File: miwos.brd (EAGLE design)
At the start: 120 x 120 mm, 50 parts, among them J1 614004190021, U1 PEC16, U3 PEC16

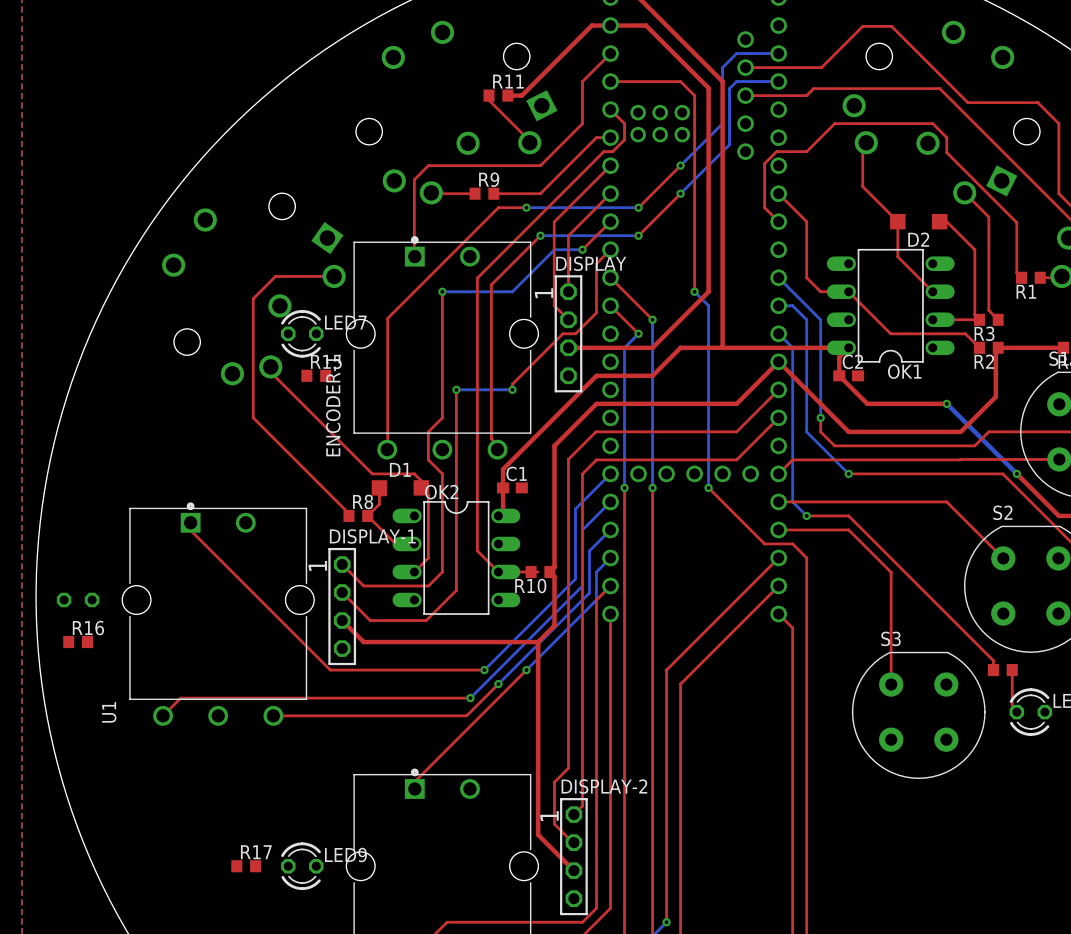
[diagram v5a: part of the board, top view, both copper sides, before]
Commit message: Wire encoder LEDs
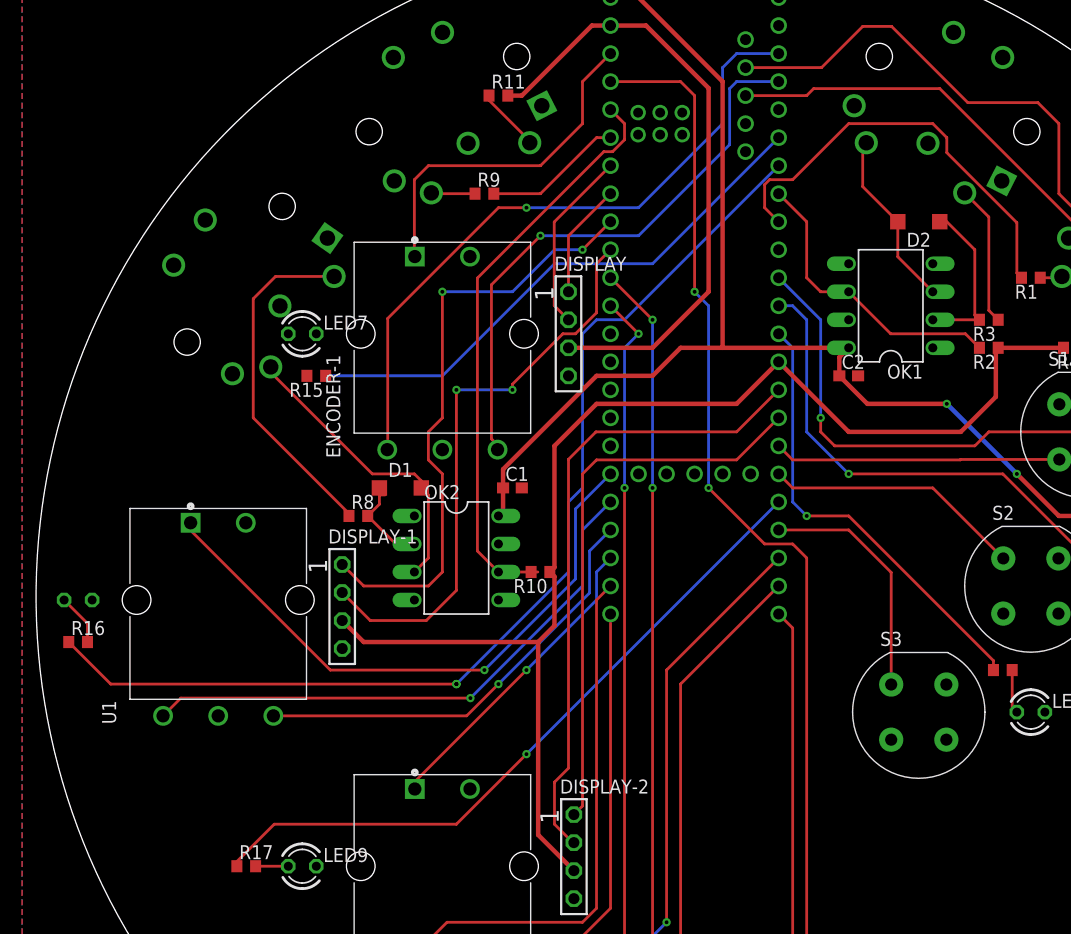
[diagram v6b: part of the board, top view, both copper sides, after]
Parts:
- turned R15 to 180 degrees
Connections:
- net BUTTON-1: now also TEENSY-41.26; no longer TEENSY-41.27
- net BUTTON-2: now also TEENSY-41.27; no longer TEENSY-41.28
- net ENCODER-1-LED: now also TEENSY-41.5
- net ENCODER-2-LED: now also TEENSY-41.6
- net ENCODER-3-LED: now also TEENSY-41.28
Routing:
- net ENCODER-2-LED: track 0.00 -> 97.3 mm, vias 0 -> 2
- net ENCODER-3-LED: track 0.00 -> 63.0 mm, vias 0 -> 1
- net ENCODER-1-LED: track 0.00 -> 49.6 mm
- net N$20: track 0.00 -> 4.69 mm
- net N$22: track 0.00 -> 2.96 mm
- net TX-2: track 39.8 -> 38.7 mm
- net BUTTON-2: track 22.5 -> 23.5 mm
- net ENCODER-1-B: vias 3 -> 1
- net ENCODER-1-A: vias 3 -> 1
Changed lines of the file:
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@@
 <attribute name="VALUE" x="26.035" y="82.169" size="1.27" layer="27" ratio="10"/>
 </element>
-<element name="R15" library="rcl" library_urn="urn:adsk.eagle:library:334" package="R0603" package3d_urn="urn:adsk.eagle:package:23555/3" value="220R" x="25.4" y="80.01" smashed="yes">
-<attribute name="NAME" x="24.765" y="80.645" size="1.27" layer="25"/>
-<attribute name="POPULARITY" value="70" x="25.4" y="76.2" size="1.778" layer="27" display="off"/>
-<attribute name="SPICEPREFIX" value="R" x="25.4" y="76.2" size="1.778" layer="27" display="off"/>
-<attribute name="VALUE" x="24.765" y="78.105" size="1.27" layer="27"/>
+<element name="R15" library="rcl" library_urn="urn:adsk.eagle:library:334" package="R0603" package3d_urn="urn:adsk.eagle:package:23555/3" value="220R" x="25.4" y="80.01" smashed="yes" rot="R180">
+<attribute name="NAME" x="26.035" y="79.375" size="1.27" layer="25" rot="R180"/>
+<attribute name="POPULARITY" value="70" x="25.4" y="83.82" size="1.778" layer="27" rot="R180" display="off"/>
+<attribute name="SPICEPREFIX" value="R" x="25.4" y="83.82" size="1.778" layer="27" rot="R180" display="off"/>
+<attribute name="VALUE" x="26.035" y="81.915" size="1.27" layer="27" rot="R180"/>
 </element>
 <element name="LED8" library="led" library_urn="urn:adsk.eagle:library:259" package="LED3MM" package3d_urn="urn:adsk.eagle:package:15797/1" value="" x="3.81" y="59.69" smashed="yes" rot="MR180">
@@
 <wire x1="41.91" y1="95.25" x2="44.45" y2="95.25" width="0.254" layer="1"/>
 <via x="44.45" y="95.25" extent="1-16" drill="0.35"/>
-<wire x1="44.45" y1="95.25" x2="54.61" y2="95.25" width="0.254" layer="16"/>
-<via x="54.61" y="95.25" extent="1-16" drill="0.35"/>
-<wire x1="54.61" y1="95.25" x2="58.42" y2="99.06" width="0.254" layer="1"/>
-<via x="58.42" y="99.06" extent="1-16" drill="0.35"/>
-<wire x1="58.42" y1="99.06" x2="62.23" y2="102.87" width="0.254" layer="16"/>
-<wire x1="62.23" y1="102.87" x2="62.23" y2="107.95" width="0.254" layer="16"/>
+<wire x1="54.61" y1="95.25" x2="44.45" y2="95.25" width="0.254" layer="16"/>
+<wire x1="62.23" y1="107.95" x2="62.23" y2="102.87" width="0.254" layer="16"/>
 <wire x1="62.23" y1="107.95" x2="63.5" y2="109.22" width="0.254" layer="16"/>
 <wire x1="63.5" y1="109.22" x2="67.31" y2="109.22" width="0.254" layer="16"/>
+<wire x1="62.23" y1="102.87" x2="54.61" y2="95.25" width="0.254" layer="16"/>
 </signal>
 <signal name="ENCODER-1-B">
@@
 <via x="45.72" y="92.71" extent="1-16" drill="0.35"/>
 <wire x1="45.72" y1="92.71" x2="54.61" y2="92.71" width="0.254" layer="16"/>
-<via x="54.61" y="92.71" extent="1-16" drill="0.35"/>
-<wire x1="54.61" y1="92.71" x2="58.42" y2="96.52" width="0.254" layer="1"/>
-<via x="58.42" y="96.52" extent="1-16" drill="0.35"/>
-<wire x1="58.42" y1="96.52" x2="62.865" y2="100.965" width="0.254" layer="16"/>
 <wire x1="62.865" y1="106.045" x2="63.5" y2="106.68" width="0.254" layer="16"/>
 <wire x1="63.5" y1="106.68" x2="67.31" y2="106.68" width="0.254" layer="16"/>
 <wire x1="62.865" y1="100.965" x2="62.865" y2="106.045" width="0.254" layer="16"/>
+<wire x1="54.61" y1="92.71" x2="62.865" y2="100.965" width="0.254" layer="16"/>
 </signal>
 <signal name="ENCODER-1-PUSH">
@@
 <contactref element="S1" pad="1"/>
 <contactref element="S1" pad="2"/>
-<contactref element="TEENSY-41" pad="27"/>
 <wire x1="92.75" y1="72.43" x2="83.82" y2="72.43" width="0.254" layer="1"/>
-<wire x1="83.78" y1="72.39" x2="68.58" y2="72.39" width="0.254" layer="1"/>
-<wire x1="67.31" y1="71.12" x2="68.58" y2="72.39" width="0.254" layer="1"/>
+<wire x1="68.58" y1="72.39" x2="83.78" y2="72.39" width="0.254" layer="1"/>
 <wire x1="83.78" y1="72.39" x2="83.82" y2="72.43" width="0.254" layer="1"/>
+<contactref element="TEENSY-41" pad="26"/>
+<wire x1="67.31" y1="73.66" x2="68.58" y2="72.39" width="0.254" layer="1"/>
 <wire x1="92.75" y1="72.43" x2="92.75" y2="77.43" width="0" layer="19" extent="1-1"/>
 </signal>
@@
 <contactref element="S2" pad="1"/>
 <contactref element="S2" pad="2"/>
-<wire x1="85.09" y1="66.04" x2="87.63" y2="63.5" width="0.254" layer="1"/>
-<contactref element="TEENSY-41" pad="28"/>
-<wire x1="87.63" y1="63.5" x2="87.67" y2="63.46" width="0.254" layer="1"/>
-<wire x1="67.31" y1="68.58" x2="82.55" y2="68.58" width="0.254" layer="1"/>
-<wire x1="82.55" y1="68.58" x2="85.09" y2="66.04" width="0.254" layer="1"/>
+<wire x1="87.67" y1="63.46" x2="81.28" y2="69.85" width="0.254" layer="1"/>
+<contactref element="TEENSY-41" pad="27"/>
+<wire x1="68.58" y1="69.85" x2="67.31" y2="71.12" width="0.254" layer="1"/>
+<wire x1="81.28" y1="69.85" x2="68.58" y2="69.85" width="0.254" layer="1"/>
 <wire x1="87.67" y1="63.46" x2="87.67" y2="58.46" width="0" layer="19" extent="1-1"/>
 </signal>
@@
 <wire x1="66.04" y1="95.25" x2="67.31" y2="93.98" width="0.254" layer="1"/>
 <wire x1="82.55" y1="101.6" x2="82.55" y2="100.242" width="0.254" layer="1"/>
-<wire x1="72.39" y1="102.87" x2="81.28" y2="102.87" width="0.254" layer="1"/>
+<wire x1="73.66" y1="102.87" x2="81.28" y2="102.87" width="0.254" layer="1"/>
 <wire x1="81.28" y1="102.87" x2="82.55" y2="101.6" width="0.254" layer="1"/>
-<wire x1="72.39" y1="102.87" x2="69.85" y2="100.33" width="0.254" layer="1"/>
-<wire x1="67.11855" y1="100.33" x2="66.04" y2="99.25145" width="0.254" layer="1"/>
-<wire x1="69.85" y1="100.33" x2="67.11855" y2="100.33" width="0.254" layer="1"/>
-<wire x1="66.04" y1="99.25145" x2="66.04" y2="95.25" width="0.254" layer="1"/>
+<wire x1="73.66" y1="102.87" x2="68.58" y2="97.79" width="0.254" layer="1"/>
+<wire x1="66.48355" y1="97.79" x2="66.04" y2="97.34645" width="0.254" layer="1"/>
+<wire x1="68.58" y1="97.79" x2="66.48355" y2="97.79" width="0.254" layer="1"/>
+<wire x1="66.04" y1="97.34645" x2="66.04" y2="95.25" width="0.254" layer="1"/>
 </signal>
 <signal name="BUTTON-4-LED">
@@
 <contactref element="LED7" pad="A"/>
 <contactref element="R15" pad="2"/>
-<wire x1="26.25" y1="80.01" x2="22.86" y2="83.82" width="0" layer="19" extent="1-1"/>
+<wire x1="24.55" y1="80.01" x2="22.86" y2="83.82" width="0" layer="19" extent="1-1"/>
 </signal>
 <signal name="N$20">
 <contactref element="LED8" pad="A"/>
 <contactref element="R16" pad="2"/>
-<wire x1="4.66" y1="55.88" x2="2.54" y2="59.69" width="0" layer="19" extent="1-1"/>
+<wire x1="2.54" y1="59.69" x2="4.66" y2="57.57" width="0.254" layer="1"/>
+<wire x1="4.66" y1="57.57" x2="4.66" y2="55.88" width="0.254" layer="1"/>
 </signal>
 <signal name="N$22">
 <contactref element="LED9" pad="A"/>
 <contactref element="R17" pad="2"/>
-<wire x1="19.9" y1="35.56" x2="22.86" y2="35.56" width="0" layer="19" extent="1-1"/>
+<wire x1="19.9" y1="35.56" x2="22.86" y2="35.56" width="0.254" layer="1"/>
 </signal>
 <signal name="ENCODER-1-LED">
 <contactref element="R15" pad="1"/>
+<contactref element="TEENSY-41" pad="5"/>
+<wire x1="67.31" y1="101.6" x2="55.88" y2="90.17" width="0.254" layer="16"/>
+<wire x1="55.88" y1="90.17" x2="46.99" y2="90.17" width="0.254" layer="16"/>
+<wire x1="46.99" y1="90.17" x2="36.83" y2="80.01" width="0.254" layer="16"/>
+<wire x1="36.83" y1="80.01" x2="26.67" y2="80.01" width="0.254" layer="16"/>
+<wire x1="26.67" y1="80.01" x2="26.25" y2="80.01" width="0" layer="19" extent="1-16"/>
 </signal>
 <signal name="ENCODER-2-LED">
 <contactref element="R16" pad="1"/>
+<contactref element="TEENSY-41" pad="6"/>
+<wire x1="67.31" y1="99.06" x2="53.34" y2="85.09" width="0.254" layer="16"/>
+<wire x1="53.34" y1="85.09" x2="50.8" y2="85.09" width="0.254" layer="16"/>
+<wire x1="50.8" y1="85.09" x2="49.53" y2="83.82" width="0.254" layer="16"/>
+<wire x1="49.53" y1="83.82" x2="49.53" y2="69.85" width="0.254" layer="16"/>
+<wire x1="49.53" y1="69.85" x2="48.26" y2="68.58" width="0.254" layer="16"/>
+<wire x1="48.26" y1="68.58" x2="48.26" y2="62.23" width="0.254" layer="16"/>
+<wire x1="48.26" y1="62.23" x2="38.1" y2="52.07" width="0.254" layer="16"/>
+<via x="38.1" y="52.07" extent="1-16" drill="0.35"/>
+<via x="38.1" y="52.07" extent="1-16" drill="0.35"/>
+<wire x1="38.1" y1="52.07" x2="6.77" y2="52.07" width="0.254" layer="1"/>
+<wire x1="6.77" y1="52.07" x2="2.96" y2="55.88" width="0.254" layer="1"/>
 </signal>
 <signal name="ENCODER-3-LED">
 <contactref element="R17" pad="1"/>
+<contactref element="TEENSY-41" pad="28"/>
+<wire x1="67.31" y1="68.58" x2="44.45" y2="45.72" width="0.254" layer="16"/>
+<via x="44.45" y="45.72" extent="1-16" drill="0.35"/>
+<wire x1="44.45" y1="45.72" x2="38.1" y2="39.37" width="0.254" layer="1"/>
+<wire x1="38.1" y1="39.37" x2="21.59" y2="39.37" width="0.254" layer="1"/>
+<wire x1="21.59" y1="39.37" x2="18.2" y2="35.98" width="0.254" layer="1"/>
+<wire x1="18.2" y1="35.98" x2="18.2" y2="35.56" width="0.254" layer="1"/>
 </signal>
 </signals>

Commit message: Use center origin, small fixes
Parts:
- moved D2 84.4 mm to (20.3, 34.3)
- moved R16 84.4 mm to (-55.9, -3.81)
- moved R5 84.4 mm to (43.2, 11.4)
- moved C1 84.4 mm to (-16.5, 10.2)
- moved C2 84.4 mm to (14.0, 20.3)
- moved D1 84.4 mm to (-26.7, 10.2)
- moved DISPLAY 84.4 mm to (-11.4, 24.1)
- moved DISPLAY-1 84.4 mm to (-31.9, -0.59)
- moved DISPLAY-2 84.4 mm to (-10.9, -23.3)
- moved ENCODER-1 84.4 mm to (-22.9, 24.1)
- moved J1 84.4 mm to (48.9, 0.67)
- moved LED1 84.4 mm to (45.7, 15.2)
- moved LED2 84.4 mm to (40.6, 1.27)
- moved LED3 84.4 mm to (30.5, -10.2)
- moved LED4 84.4 mm to (-16.5, -53.3)
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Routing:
- net N$4: track 0.00 -> 4.51 mm
- net +3V3: track 173.4 -> 174.0 mm
- net ENCODER-2-LED: track 97.3 -> 96.9 mm, vias 2 -> 1

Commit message: Place labels, small fixes
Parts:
- removed DISPLAY-1, DISPLAY-2: OLED-DISPLAY, oled-display:OLED-DISPLAY
- removed J1: 614004190021, 614004190021:614004190021
- removed S4, S5, S6: D6R90_F1_LFS, D6R90_F1_LFS:SW_D6R90_F1_LFS
- added BUTTON4, BUTTON5, BUTTON6: D6R90_F1_LFS, D6R90_F1_LFS:SW_D6R90_F1_LFS
- added DISPLAY2, DISPLAY3: OLED-DISPLAY, oled-display:OLED-DISPLAY
- added USB-HUB: 614004190021, 614004190021:614004190021
- moved R13 1.27 mm to (-3.81, -53.3)
- moved LED6 1.27 mm to (16.5, -53.3)
- moved R12 1.27 mm to (-12.7, -53.3)
- flipped LED8 to the top, turned to 0 degrees
- renumbered DISPLAY to DISPLAY1, ENCODER-1 to ENCODER1, MIDI-IN-1 to MIDI2-IN, MIDI-IN-2 to MIDI1-IN, MIDI-OUT-1 to MIDI2-OUT, MIDI-OUT-2 to MIDI1-OUT, S1 to BUTTON1, S2 to BUTTON2, S3 to BUTTON3, U1 to ENCODER2, U3 to ENCODER3
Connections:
- net BUTTON-1 renamed BUTTON1
- net BUTTON-1-LED renamed BUTTON1-LED
- net BUTTON-2 renamed BUTTON2
- net BUTTON-2-LED renamed BUTTON2-LED
- net BUTTON-3 renamed BUTTON3
- net BUTTON-3-LED renamed BUTTON3-LED
- net BUTTON-4-LED renamed BUTTON4-LED
- net BUTTON-5-LED renamed BUTTON5-LED
- net BUTTON-6-LED renamed BUTTON6-LED
- net ENCODER-1-A renamed ENCODER1-A
- net ENCODER-1-B renamed ENCODER1-B
- net ENCODER-1-LED renamed ENCODER1-LED
- net ENCODER-1-PUSH renamed ENCODER1-PUSH
- net ENCODER-2-A renamed ENCODER2-A
- net ENCODER-2-B renamed ENCODER2-B
- net ENCODER-2-LED renamed ENCODER2-LED
- net ENCODER-2-PUSH renamed ENCODER2-PUSH
- net ENCODER-3-A renamed ENCODER3-A
- net ENCODER-3-B renamed ENCODER3-B
- net ENCODER-3-LED renamed ENCODER3-LED
- net ENCODER-3-PUSH renamed ENCODER3-PUSH
- net RX-1 renamed RX1
- net RX-2 renamed RX2
- net RX-5 renamed RX5
- net TX-1 renamed TX1
- net TX-2 renamed TX2
- net TX-5 renamed TX5
- removed net BUTTON-4: S4.1, S4.2, TEENSY-41.30
- removed net BUTTON-5: S5.1, S5.2, TEENSY-41.31/A12
- removed net BUTTON-6: S6.1, S6.2, TEENSY-41.32
- removed net SCL-1: DISPLAY-1.2, TEENSY-41.16/A2
- removed net SCL-2: DISPLAY-2.2, TEENSY-41.24
- removed net SDA-1: DISPLAY-1.1, TEENSY-41.17/A3
- removed net SDA-2: DISPLAY-2.1, TEENSY-41.25
- new net BUTTON4: BUTTON4.1, BUTTON4.2, TEENSY-41.30
- new net BUTTON5: BUTTON5.1, BUTTON5.2, TEENSY-41.31/A12
- new net BUTTON6: BUTTON6.1, BUTTON6.2, TEENSY-41.32
- new net SCL1: DISPLAY2.2, TEENSY-41.16/A2
- new net SCL2: DISPLAY3.2, TEENSY-41.24
- new net SDA1: DISPLAY2.1, TEENSY-41.17/A3
- new net SDA2: DISPLAY3.1, TEENSY-41.25
- net +3V3: now also DISPLAY2.3, DISPLAY3.3; no longer DISPLAY-1.3, DISPLAY-2.3
- net +5V: now also USB-HUB.1; no longer J1.1
- net GND: now also BUTTON4.3, BUTTON4.4, BUTTON5.3, BUTTON5.4, BUTTON6.3, BUTTON6.4, DISPLAY2.4, DISPLAY3.4, USB-HUB.4; no longer DISPLAY-1.4, DISPLAY-2.4, J1.4, S4.3, S4.4, S5.3, S5.4, S6.3, S6.4
- net N$2: now also USB-HUB.2; no longer J1.2
- net N$3: now also USB-HUB.3; no longer J1.3
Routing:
- net BUTTON-4: track 58.8 -> 0.00 mm, vias 2 -> 0
- net BUTTON4: track 0.00 -> 58.4 mm, vias 0 -> 2
- net SCL2: track 0.00 -> 58.3 mm
- net SCL-2: track 57.7 -> 0.00 mm
- net SDA1: track 0.00 -> 54.8 mm, vias 0 -> 2
- net SDA-1: track 54.7 -> 0.00 mm, vias 2 -> 0
- net SCL1: track 0.00 -> 52.9 mm, vias 0 -> 2
- net SCL-1: track 52.8 -> 0.00 mm, vias 2 -> 0
- net SDA2: track 0.00 -> 52.2 mm
- net SDA-2: track 51.1 -> 0.00 mm
- net BUTTON-5: track 46.5 -> 0.00 mm
- net BUTTON5: track 0.00 -> 46.1 mm
- net BUTTON-6: track 42.9 -> 0.00 mm
- net BUTTON6: track 0.00 -> 42.1 mm
- net +3V3: track 174.0 -> 182.8 mm
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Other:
- board text added: "3V"
- board text added: "5V"
- board text added: "MIDI1-IN"
- board text added: "MIDI1-OUT"
- board text added: "MIDI2-IN"
- board text added: "MIDI2-OUT"
- board text added: "RX5"
- board text added: "SCL"
- board text added: "SCL1"
- board text added: "SCL2"
- board text added: "SDA"
- board text added: "SDA1"
- board text added: "SDA2"
- board text added: "TX5"
- board text added: "UD+"
- board text added: "UD-"
- board text added: "USB-HUB"
- board text added: "USB/POWER"
- board text added: "VIN"
